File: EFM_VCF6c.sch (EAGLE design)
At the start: 69 parts, among them IC1 LM13700N, Q1 2N3904, Q2 2N3904, Q3 2N3906, Q4 2N3904, Q5 2N3906, U1 POWER

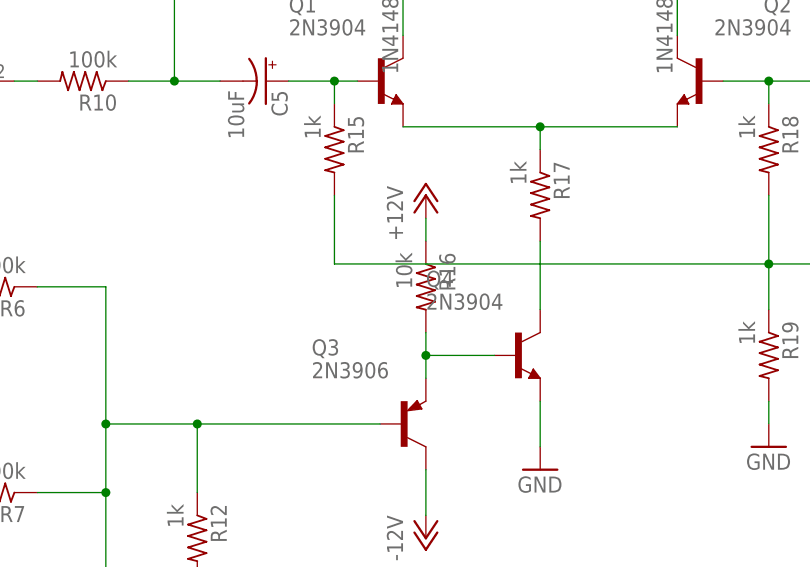
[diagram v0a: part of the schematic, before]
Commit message: fixed cv range setting r16
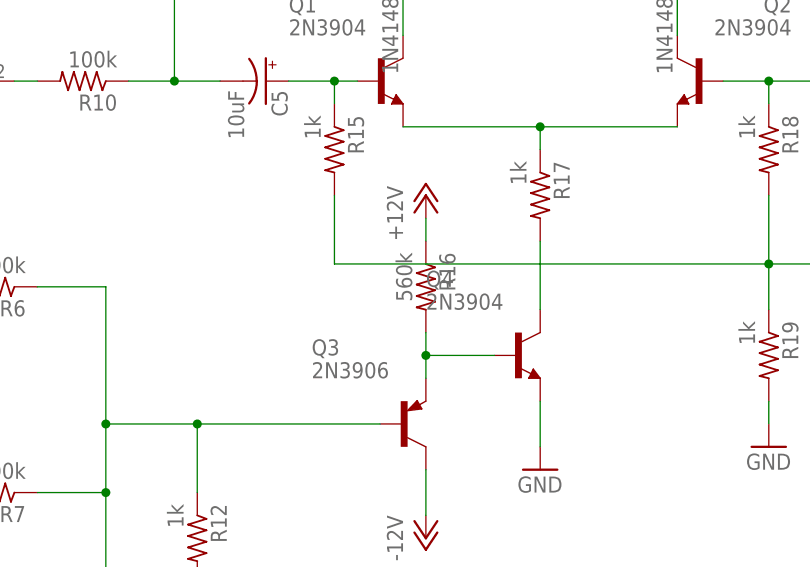
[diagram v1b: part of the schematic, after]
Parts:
- R16: value 10k -> 560k
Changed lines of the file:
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@@
 <part name="R17" library="rcl" deviceset="R-US_" device="0207/7" value="1k"/>
 <part name="GND10" library="supply1" deviceset="GND" device=""/>
-<part name="R16" library="rcl" deviceset="R-US_" device="0207/7" value="10k"/>
+<part name="R16" library="rcl" deviceset="R-US_" device="0207/7" value="560k"/>
 <part name="P+7" library="supply1" deviceset="+12V" device=""/>
 <part name="P-5" library="supply1" deviceset="-12V" device=""/>

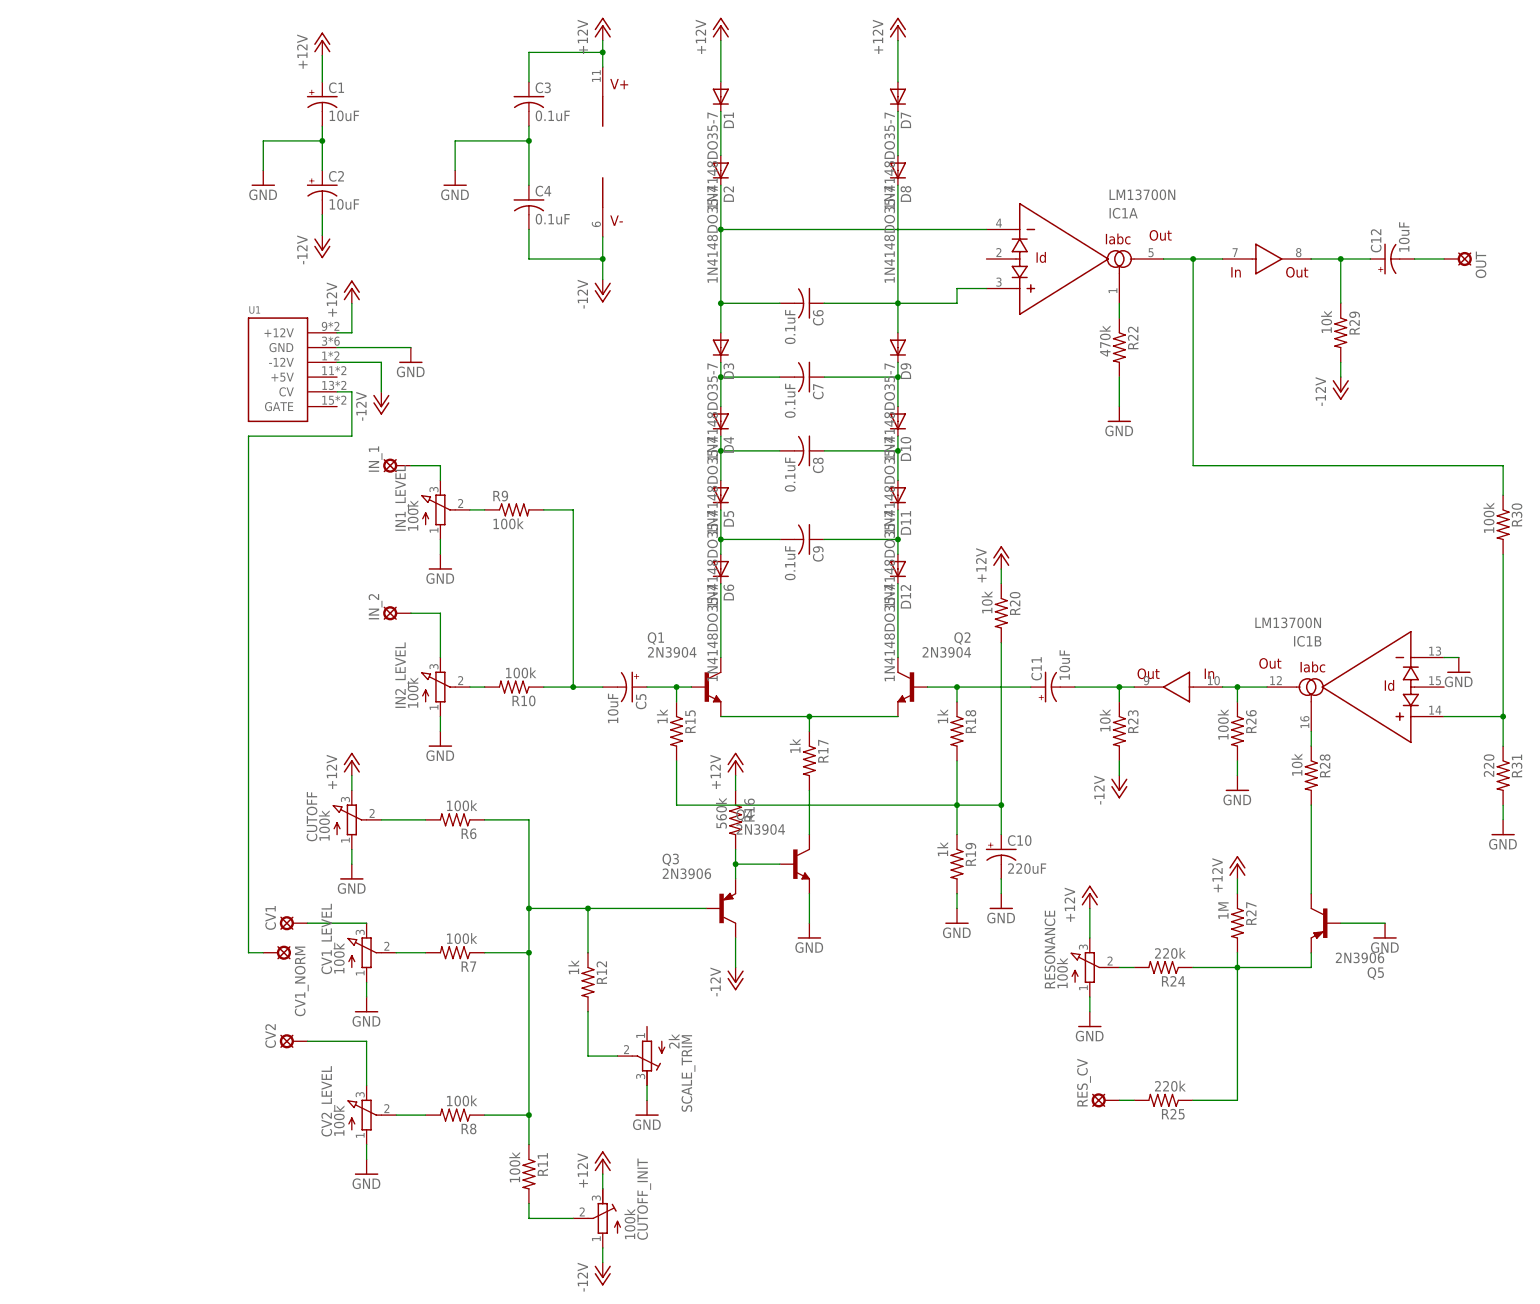
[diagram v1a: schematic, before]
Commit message: updated power and pots and better diodes
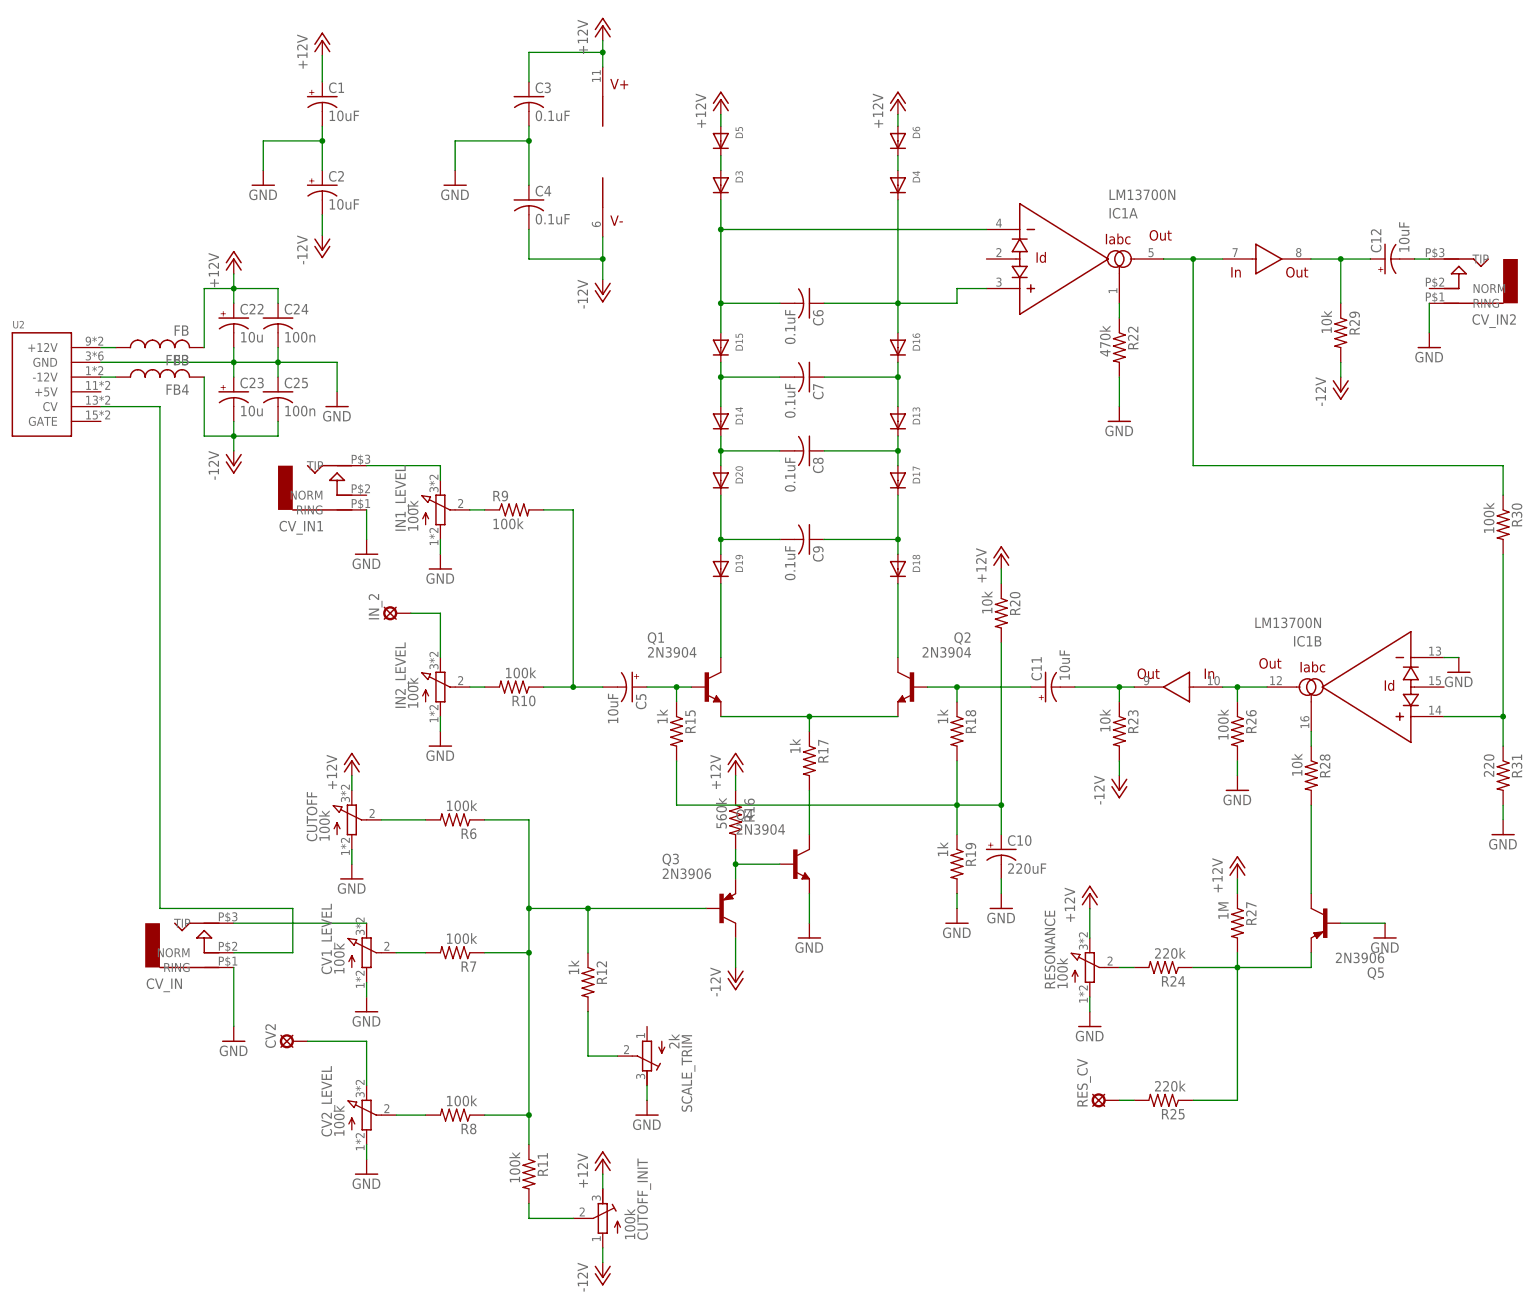
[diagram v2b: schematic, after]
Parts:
- removed CV1, CV1_NORM, IN_1, OUT: LSP10, solpad:LSP10
- removed D1, D10, D11, D12, D2, D7, D8, D9: 1N4148DO35-7, diode:1N4148DO35-7
- removed U1: POWER, eurorack:POWER
- added C22, C23: 10u, rcl:CPOL-USB45181A
- added C24, C25: 100n, rcl:C-US050-024X044
- added CV_IN, CV_IN1, CV_IN2: AUDIO-JACKITEAD, erthenvar:AUDIO-JACKITEAD
- added D13, D14, D15, D16, D17, D18, D19, D20: (no value), adafruit:DIODEDO-1N4148
- added FB3, FB4: FB, adafruit:FB
- added U2: POWER, eurorack:POWER
- C3, C4: device rcl:C-US025-030X050 -> rcl:C-USC1206
- D3, D4, D5, D6: value 1N4148DO35-7 -> (none); device diode:1N4148DO35-7 -> adafruit:DIODEDO-1N4148
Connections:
- removed net N$55: CV1_NORM.MP, U1.CV
- new net +12V: C22.+, C24.1, FB3.2
- new net N$39: CV_IN.NORM, U2.CV
- new net N$41: FB3.1, U2.+12V
- new net N$68: FB4.1, U2.-12V
- net -12V: now also C23.-, C25.2, FB4.2; no longer U1.-12V
- net GND: now also C22.-, C23.+, C24.2, C25.1, CV_IN.RING, CV_IN1.RING, CV_IN2.RING, U2.GND; no longer U1.GND
- net N$12: now also D16.A, D4.C; no longer D8.C, D9.A
- net N$13: now also D13.A, D16.C; no longer D10.A, D9.C
- net N$14: now also D14.C, D20.A; no longer D4.C, D5.A
- net N$15: now also D13.C, D17.A; no longer D10.C, D11.A
- net N$17: now also D17.C, D18.A; no longer D11.C, D12.A
- net N$18: now also D19.A, D20.C; no longer D5.C, D6.A
- net N$19: now also D19.C; no longer D6.C
- net N$20: now also D18.C; no longer D12.C
- net N$21: now also D3.A, D5.C; no longer D1.C, D2.A
- net N$22: now also D4.A, D6.C; no longer D7.C, D8.A
- net N$29: now also D14.A, D15.C; no longer D3.C, D4.A
- net N$31: now also CV_IN2.TIP; no longer OUT.MP
- net N$38: now also D5.A, D6.A; no longer D1.A, D7.A, U1.+12V
- net N$58: now also CV_IN1.TIP; no longer IN_1.MP
- net N$59: now also CV_IN.TIP; no longer CV1.MP
- net N$9: now also D15.A, D3.C; no longer D2.C, D3.A
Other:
- moved on the sheet: D3, D4, D5, D6
